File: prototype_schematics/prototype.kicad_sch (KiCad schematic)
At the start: 44 parts, among them J1 Conn_Coaxial, J2 +5V, J3 AudioJack3, U1 CD74HC4046A, U2 MAX2608EUT+T, U3 MAX2680AUT+, U4 TPA721DR, U5 RT9059GSP

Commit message: update schematics
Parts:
- added RV1: 10k, symbol Device:R_Potentiometer_US
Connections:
- net +3V0: now also C13.1, C14.1, L4.1, R6.1, U3.5 (VCC), U3.6 (*SHDN), RV1.1
- net GND: now also RV1.3
- net at C5.1, U2.3 (TUNE): now also RV1.2
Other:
- moved on the sheet: C5, L1, U3

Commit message: add if filter
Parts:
- removed R7: 5k6, symbol Device:R_US
- added R7: DNI, symbol Device:R_Small_US
- added RV2: 10k, symbol Device:R_Potentiometer_US
- added Y1: 10.7MHz, symbol Device:Resonator_Small
- C11: value 43pF -> 33pF
- L4: value 430nH -> 10uH
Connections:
- net GND: now also R7.2, Y1.2
- net at C17.1, R8.1, U4.4 (IN-): now also RV2.1
- net at C12.1, U1.14 (SigIn): now also R7.1, Y1.3; no longer C11.2
- net at C15.2: now also RV2.2, RV2.3
- new net: C11.2, Y1.1
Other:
- note added: "At 10MHz, Z_IFOUT = 1100-80j"
- moved on the sheet: C1, C12, C15, C2, C3, C4, JP1, JP2, JP3, R1, R2, R3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

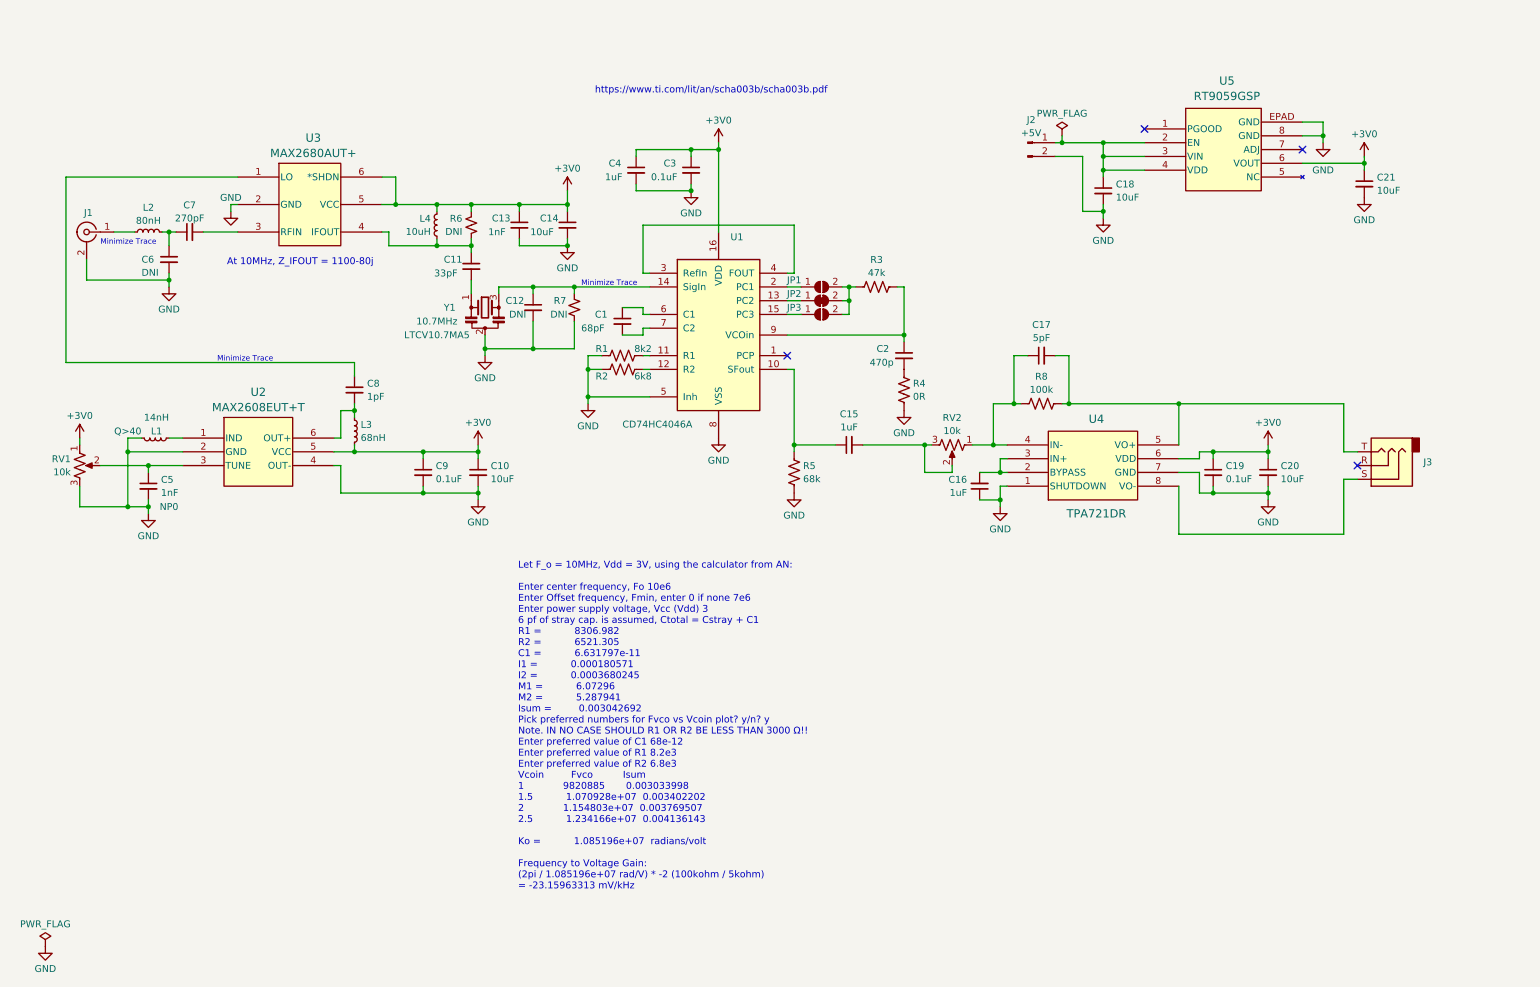
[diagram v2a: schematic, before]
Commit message: bump PLL to 20MHz and add a SAW filter
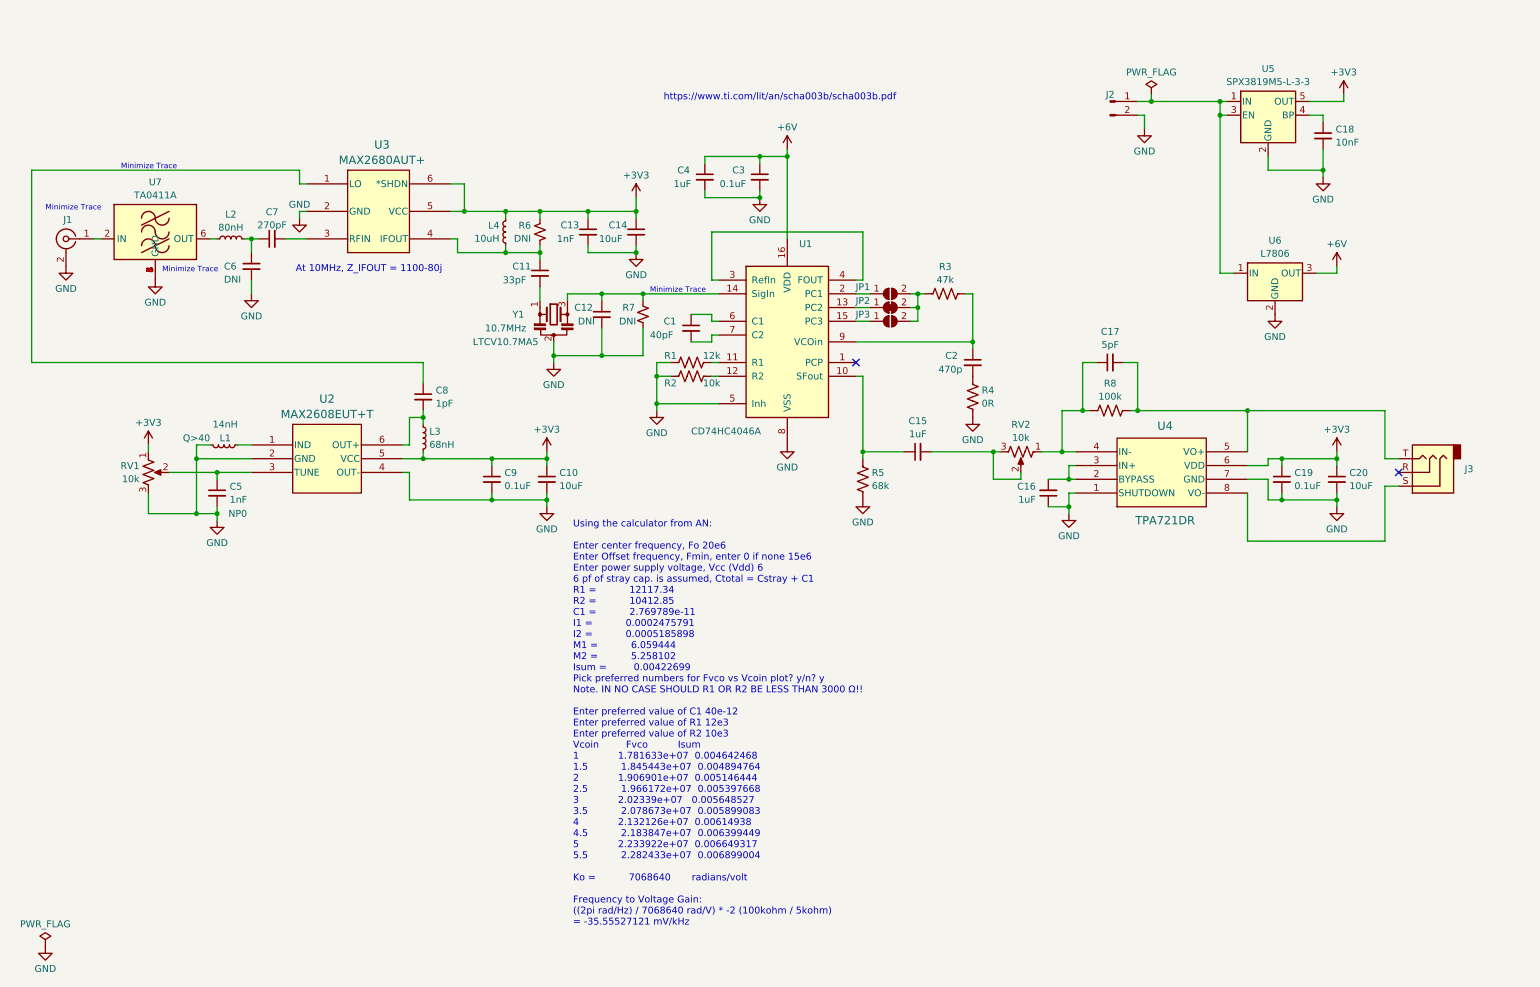
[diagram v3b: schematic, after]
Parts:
- removed C21: 10uF, symbol Device:C_Small
- removed U5: RT9059GSP, SOP8_EP_OPT1_RIT, symbol RT9059GSP:RT9059GSP
- added U5: SPX3819M5-L-3-3, Package_TO_SOT_SMD:SOT-23-5, symbol Regulator_Linear:SPX3819M5-L-3-3
- added U6: L7806, symbol Regulator_Linear:L7806
- added U7: TA0411A, RF_Mini-Circuits:Mini-Circuits_HQ1157, symbol RF_Filter:BPF-A355
- C1: value 68pF -> 40pF
- C18: value 10uF -> 10nF
- J2: value +5V -> Conn_01x02_Pin
- R1: value 8k2 -> 12k
- R2: value 6k8 -> 10k
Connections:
- net GND: now also U5.2 (GND), U6.2 (GND), U7.1 (GND), U7.3 (GND), U7.4 (GND), U7.5 (GND), U7.7 (GND), U7.8 (GND)
- net at J1.1 (In): now also U7.2 (IN); no longer L2.1
- net at J2.1 (Pin_1): now also U5.1 (IN), U5.3 (EN), U6.1 (IN); no longer C18.1
- net +3V0 renamed +3V3
- net +3V3: now also U5.5 (OUT); no longer C3.1, C4.1, U1.16 (VDD)
- new net: L2.1, U7.6 (OUT)
- new net: C18.1, U5.4 (BP)
- new net +6V: C3.1, C4.1, U1.16 (VDD), U6.3 (OUT)
- no-connect marks 4 -> 2
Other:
- moved on the sheet: C1, C10, C11, C12, C13, C14, C15, C16, C17, C19, C2, C20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

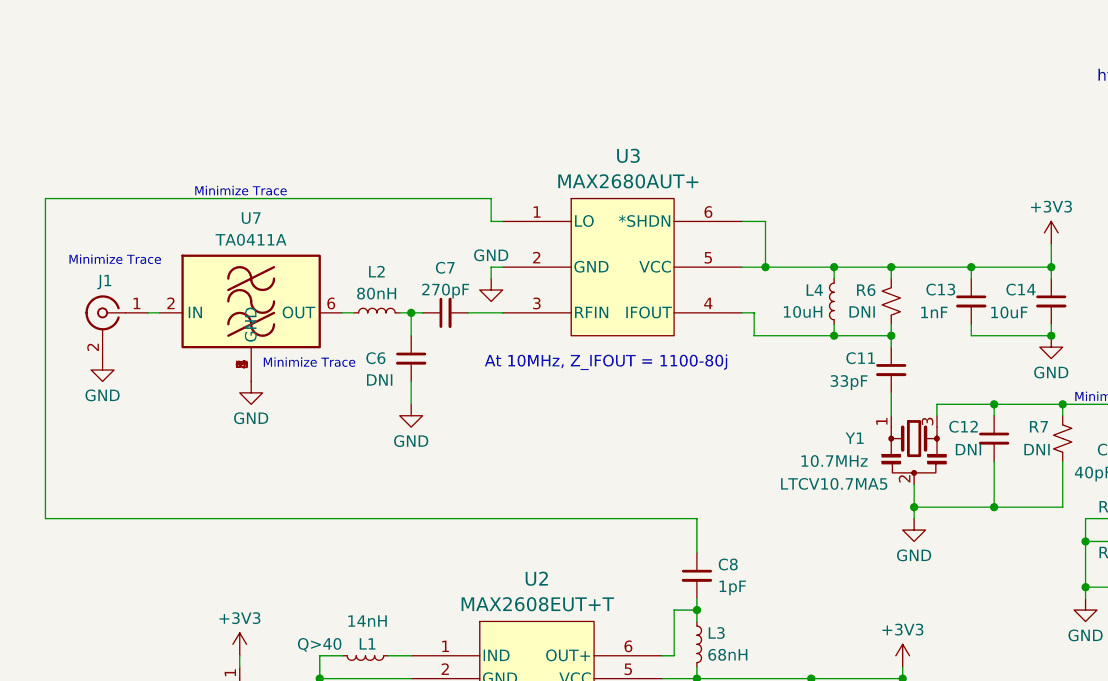
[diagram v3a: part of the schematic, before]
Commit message: add a prototype filter board
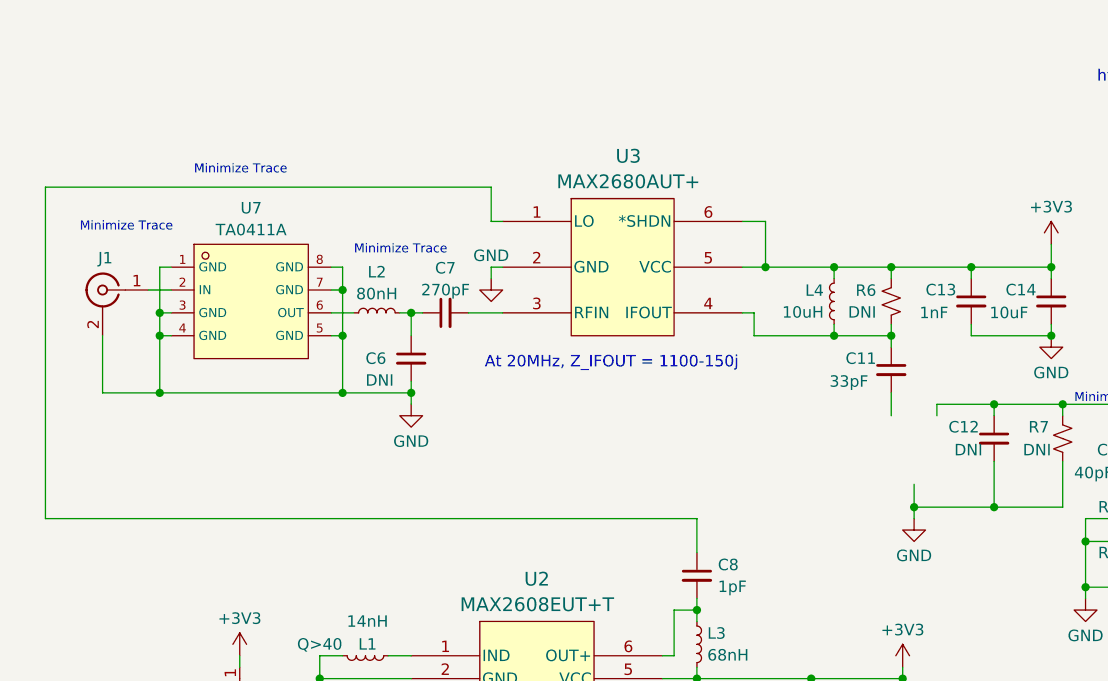
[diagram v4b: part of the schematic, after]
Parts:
- removed U7: TA0411A, RF_Mini-Circuits:Mini-Circuits_HQ1157, symbol RF_Filter:BPF-A355
- removed Y1: 10.7MHz, symbol Device:Resonator_Small
- added U7: TA0411A, footprint:FILTER-SMD_8P-L5.0-W5.0-BL, symbol TA0411A:TA0411A
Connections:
- net GND: now also U7.1 (GND), U7.3 (GND), U7.4 (GND), U7.5 (GND), U7.7 (GND), U7.8 (GND)
- net at J1.1 (In): now also U7.2 (IN)
- net at L2.1: now also U7.6 (OUT)
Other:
- note added: "At 20MHz, Z_IFOUT = 1100-150j"
- note removed: "At 10MHz, Z_IFOUT = 1100-80j"
- moved on the sheet: J1

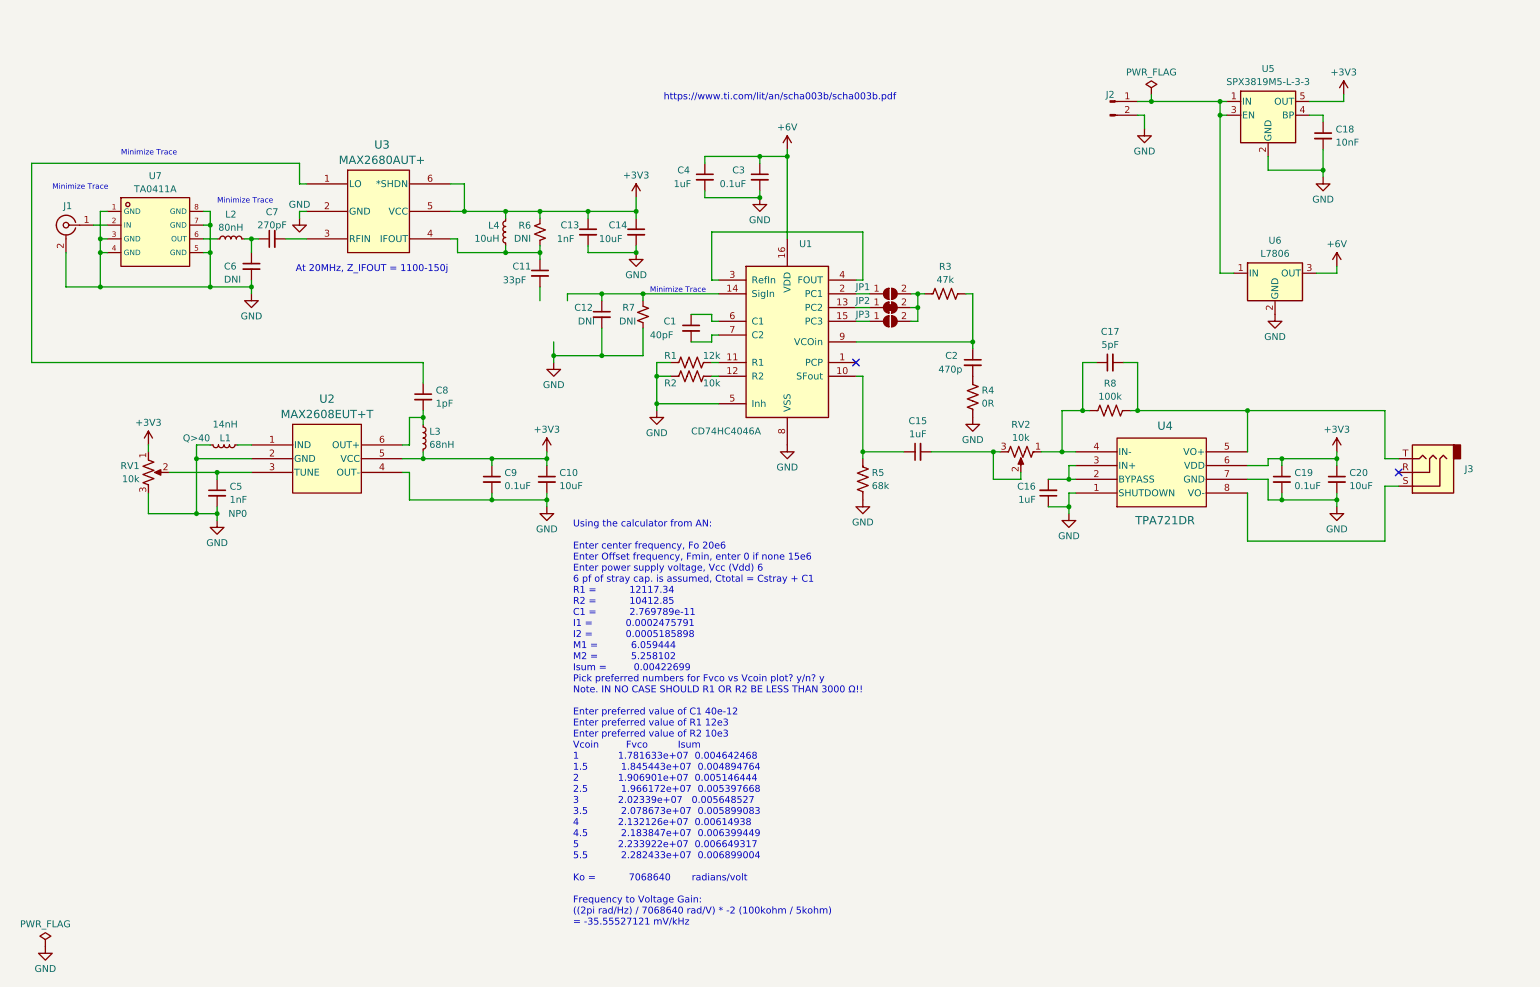
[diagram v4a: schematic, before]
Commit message: adding filters and amps
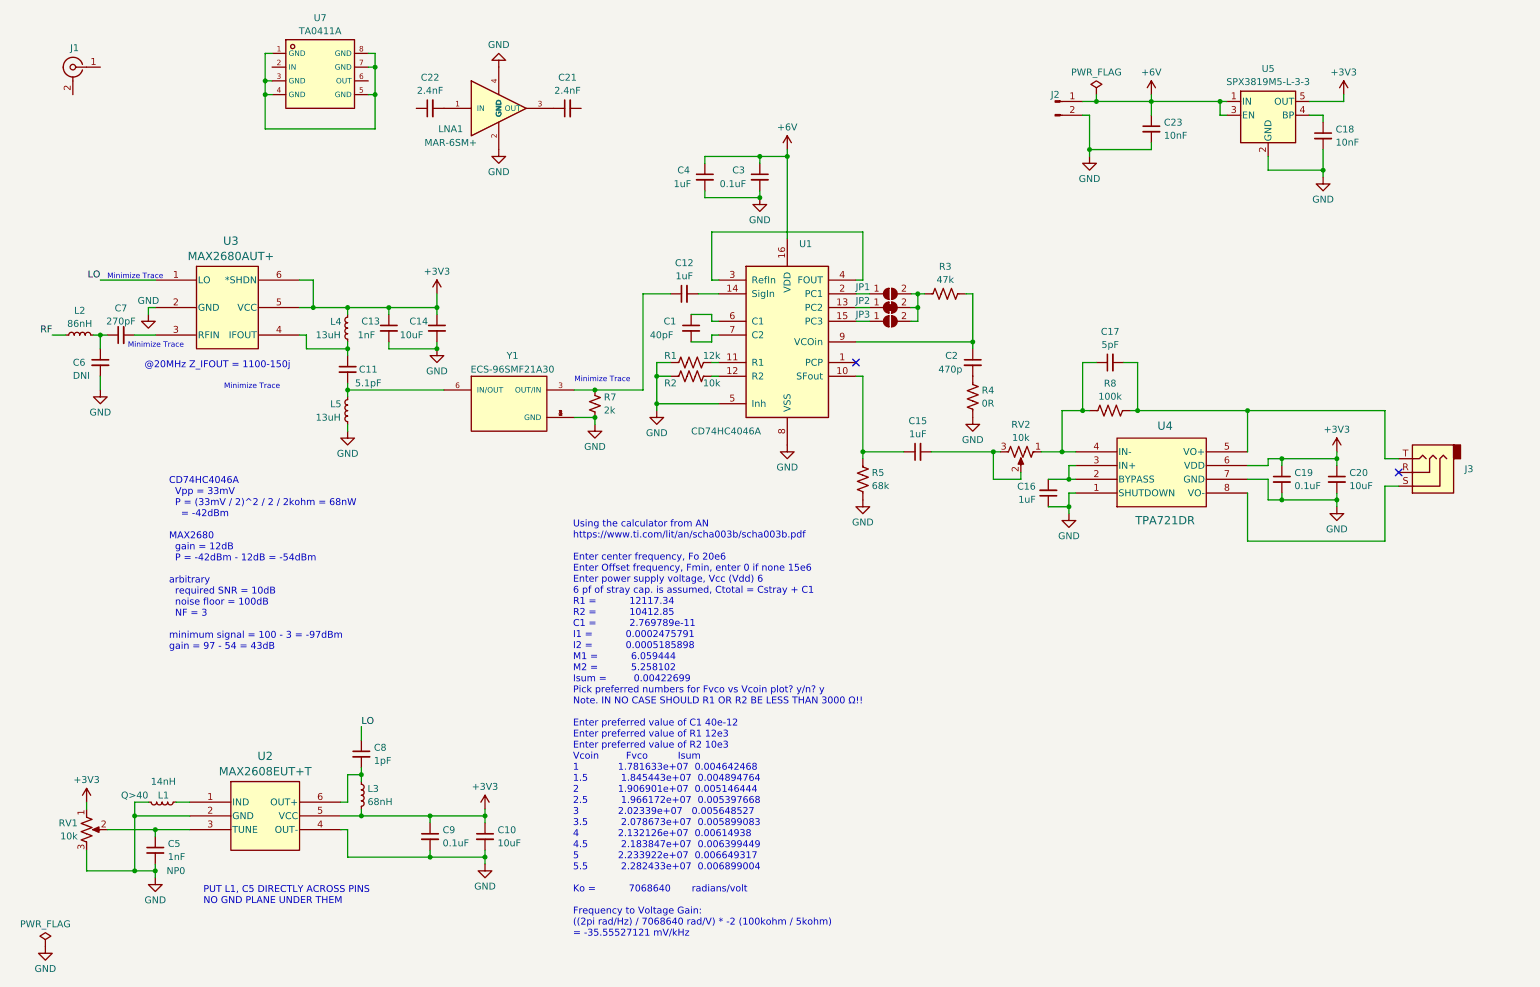
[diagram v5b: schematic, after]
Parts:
- removed R6: DNI, symbol Device:R_Small_US
- removed U6: L7806, symbol Regulator_Linear:L7806
- added C21, C22: 2.4nF, symbol Device:C_Small
- added C23: 10nF, symbol Device:C_Small
- added L5: 13uH, symbol Device:L_Small
- added LNA1: MAR-6SM+, MAR-6SM_:MAR-6SM__FOOTPRINT, symbol MAR-6SM_:MAR-6SM_
- added Y1: ECS-96SMF21A30, ECS-96SMF21A30:XTAL_ECS-96SMF21A30, symbol ECS-96SMF21A30:ECS-96SMF21A30
- C11: value 33pF -> 5.1pF
- C12: value DNI -> 1uF
- L2: value 80nH -> 86nH
- L4: value 10uH -> 13uH
- R7: value DNI -> 2k
- U1: Application Note (none) -> https://www.ti.com/lit/an/scha003b/scha003b.pdf
- U2, U3: Reference Design (none) -> https://www.analog.com/media/en/technical-documentation/dat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
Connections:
- net +6V: now also J2.1 (Pin_1), U5.1 (IN), U5.3 (EN), C23.1
- net GND: now also C23.2, L5.2, LNA1.2 (GND), LNA1.4 (GND), Y1.1 (GND), Y1.2 (GND), Y1.4 (GND), Y1.5 (GND); no longer C12.2, J1.2 (Ext), U7.1 (GND), U7.3 (GND), U7.4 (GND), U7.5 (GND), U7.7 (GND), U7.8 (GND)
- net at U7.2 (IN): no longer J1.1 (In)
- net at U7.6 (OUT): no longer L2.1
- net at C12.1, R7.1: now also Y1.3 (OUT/IN); no longer U1.14 (SigIn)
- net LO: now reaches C8.1, U3.1 (LO)
- net at C11.2: now also L5.1, Y1.6 (IN/OUT)
- new net: U7.1 (GND), U7.3 (GND), U7.4 (GND), U7.5 (GND), U7.7 (GND), U7.8 (GND)
- new net: C22.2, LNA1.1 (IN)
- new net: C21.1, LNA1.3 (OUT)
- new net: C12.2, U1.14 (SigIn)
- new net RF: L2.1
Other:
- note added: "@20MHz Z_IFOUT = 1100-150j"
- note added: "CD74HC4046A Vpp = 33mV P = (33mV / 2)^2 / 2 / 2kohm = 68nW = -42dBm MAX2680 gain = 12dB P = -42dBm - 12dB = -54dBm arbitrary required SNR = 10dB noise floor = 100dB NF = 3 minimum signal = 100 - 3 = -97dBm gain = 97 - 54 = 43dB"
- note added: "PUT L1, C5 DIRECTLY ACROSS PINS NO GND PLANE UNDER THEM"
- note removed: "At 20MHz, Z_IFOUT = 1100-150j"
- note removed: "https://www.ti.com/lit/an/scha003b/scha003b.pdf"
- moved on the sheet: C10, C13, C14, C5, C6, C7, C8, C9, J1, J2, L1, L2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
